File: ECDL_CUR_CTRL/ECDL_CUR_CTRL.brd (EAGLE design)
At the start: 92.5 x 94.5 mm, 185 parts, among them IC1 LM317MDT, IC10 74LVC1G125DCKR, IC2 LM399H, IC3 OPA2227D, IC5 LM340S-12, IC6 L7912, IC7 AD8676, IC8 TL071D, IC9 AD8676, Q1 IRF9Z14, Q2 2N7002, Q3 SSM3J328R,LF, U1 ATSAMD21G-A, U3 AD5541, U4 TS514AID, U5 LM1117IMP-3.3, U6 LM1117IMP-5.0, Y1 32,768Khz_SMD

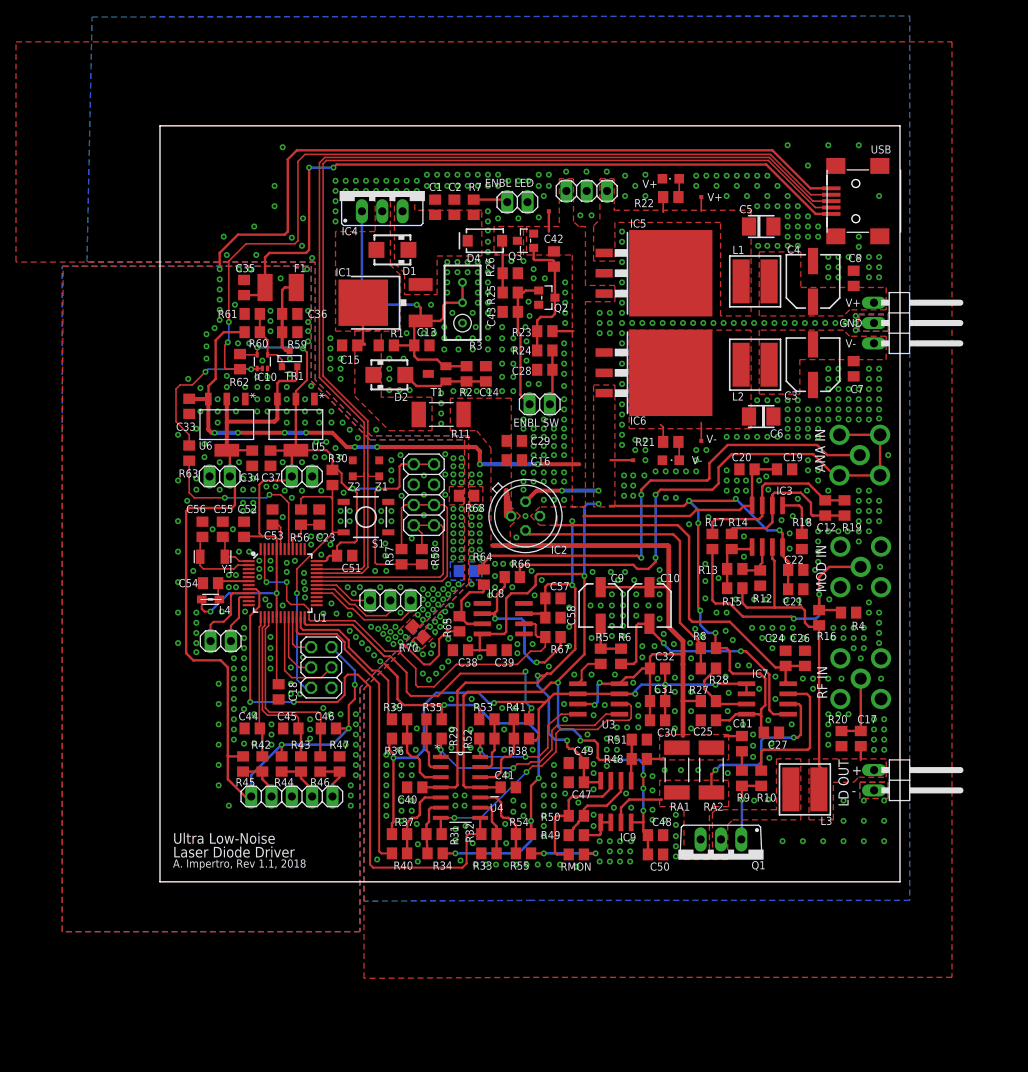
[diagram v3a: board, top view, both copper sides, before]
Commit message: Changes to Analog PID. Added LTC1923 Design.
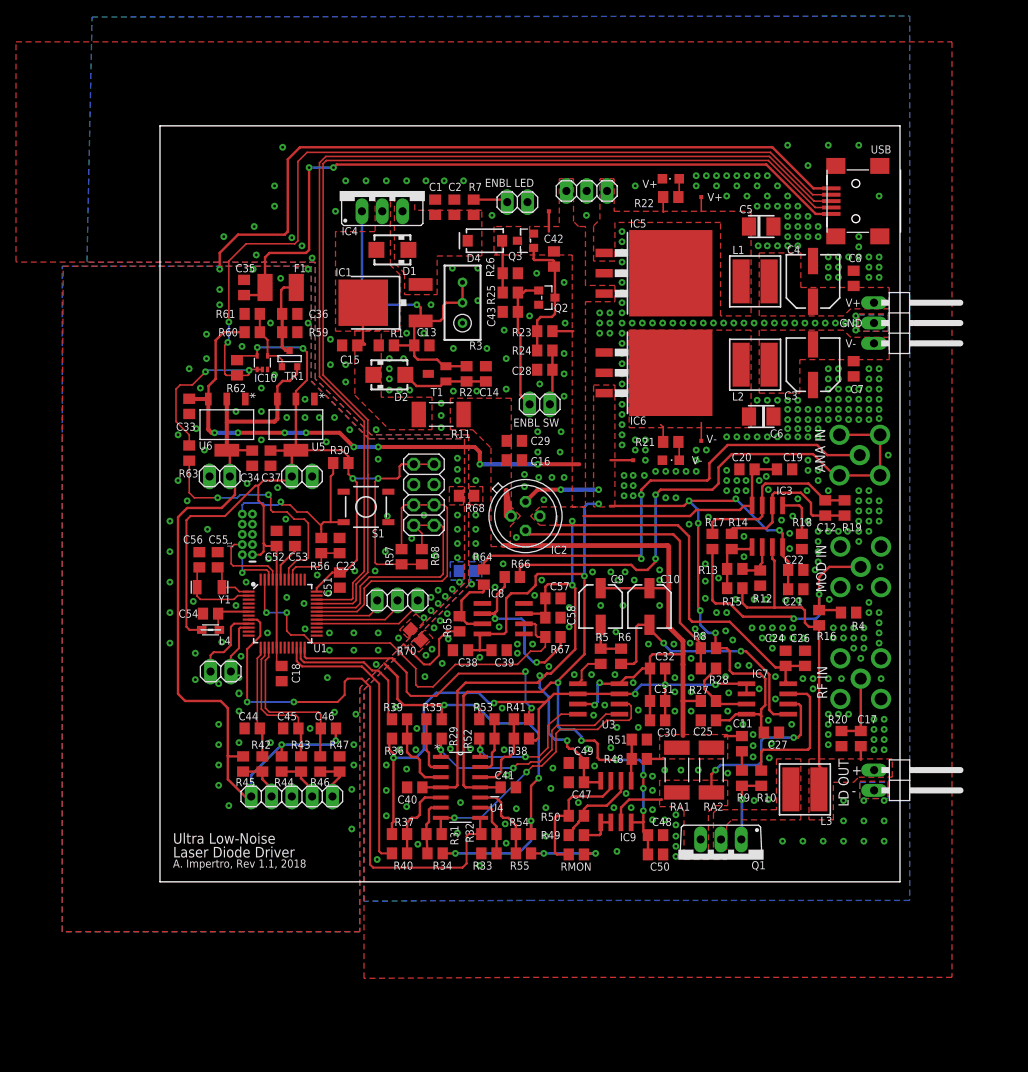
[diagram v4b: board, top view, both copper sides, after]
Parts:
- removed JP6: (no value), pinhead:2X03
- removed Z1, Z2: BRNCG0603MLC-05E, Arduino-M0-V1:PROTEZIONE_CT/CN0603
- added J1: CORTEX_DEBUG_PTH, SparkFun-Connectors:2X5-PTH-1.27MM
- C55, C56: value 100nF -> 22pF
- T1: value (none) -> MMBT2907
- moved C23 4.37 mm to (22.4, 42.0)
- moved R56 4.37 mm to (20.2, 42.0)
- moved C52 4.22 mm to (14.6, 42.9)
- moved C55 3.86 mm to (7.21, 40.3)
- moved C53 3.86 mm to (16.9, 42.9)
- moved C56 3.83 mm to (4.92, 40.3)
- moved Y1 3.83 mm to (6.19, 36.8)
- moved C54 3.81 mm to (6.32, 33.5)
- moved U1 3.81 mm to (15.3, 33.5)
- moved JP8 3.81 mm to (7.59, 26.3)
- moved L4 3.81 mm to (6.32, 31.5)
- moved C51 3.11 mm to (22.5, 37.7), turned to 270 degrees
- moved C18 2.32 mm to (15.2, 26.0)
- moved R30 2.09 mm to (22.6, 52.4), turned to 0 degrees
- moved S1 1.27 mm to (25.8, 46.9)
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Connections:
- new net SWDCLK: J1.4, U1.45
- new net SWDIO: J1.2, U1.46
- net +3V3: now also J1.1
- net +5V: no longer JP6.2
- net DGND: now also J1.3, J1.5; no longer JP6.6, Z1.2, Z2.2
- net PB10_S4_SPI_MOSI: no longer JP6.4
- net PB11_S4_SPI_SCK: no longer JP6.3
- net PB12_S4_SPI_MISO: no longer JP6.1
- net RESET: now also J1.10; no longer JP6.5
- net TARGET_USB_N: no longer Z1.1
- net TARGET_USB_P: no longer Z2.1
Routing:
- net +3V3: track 127.3 -> 144.1 mm, vias 6 -> 4
- net +5V: track 114.6 -> 100.8 mm, vias 3 -> 2
- net PB10_S4_SPI_MOSI: track 13.4 -> 0.00 mm
- net RESET: track 35.8 -> 25.3 mm
- net SWDCLK: track 0.00 -> 10.2 mm
- net PB11_S4_SPI_SCK: track 8.35 -> 0.00 mm
- net PA28_USB_HOST_EN: track 23.1 -> 30.4 mm
- net SWDIO: track 0.00 -> 6.81 mm, vias 0 -> 1
- net PB12_S4_SPI_MISO: track 5.82 -> 0.00 mm
- net DCURMON: track 76.1 -> 72.3 mm
- net ENCBTN: track 24.0 -> 20.2 mm
- net ENCA: track 21.9 -> 18.2 mm
- net ENCB: track 17.6 -> 14.0 mm
- net SCL: track 29.0 -> 31.9 mm
- net SDA: track 36.3 -> 39.0 mm
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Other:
- board text added: "SWD"
- board text removed: "ICSP"
